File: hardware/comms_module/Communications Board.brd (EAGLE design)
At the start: 33.5 x 32.4 mm, 68 parts, among them U1 Value, U2 STC3115, X2 USB-MICROB, Y1 32.768kHz, Y2 24MHz

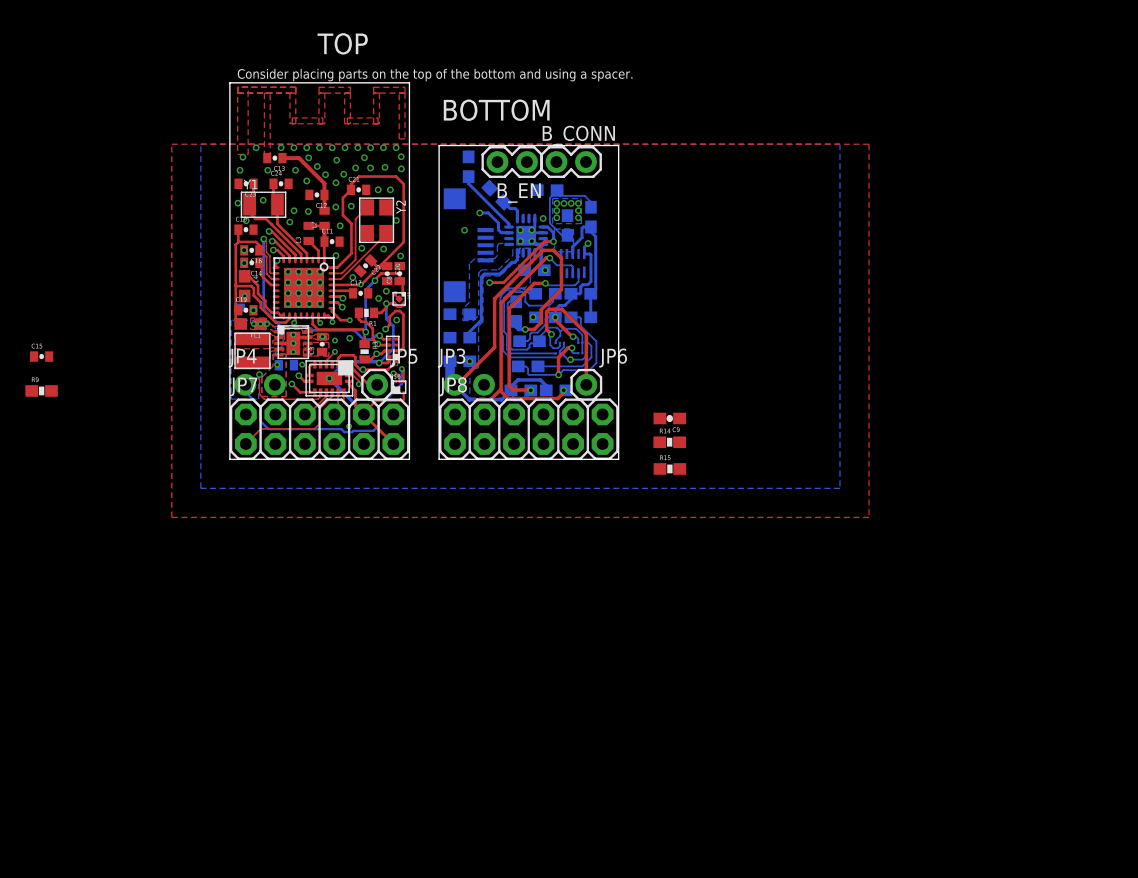
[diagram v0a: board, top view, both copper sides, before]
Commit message: Nearly complete routing. Add programming interface.
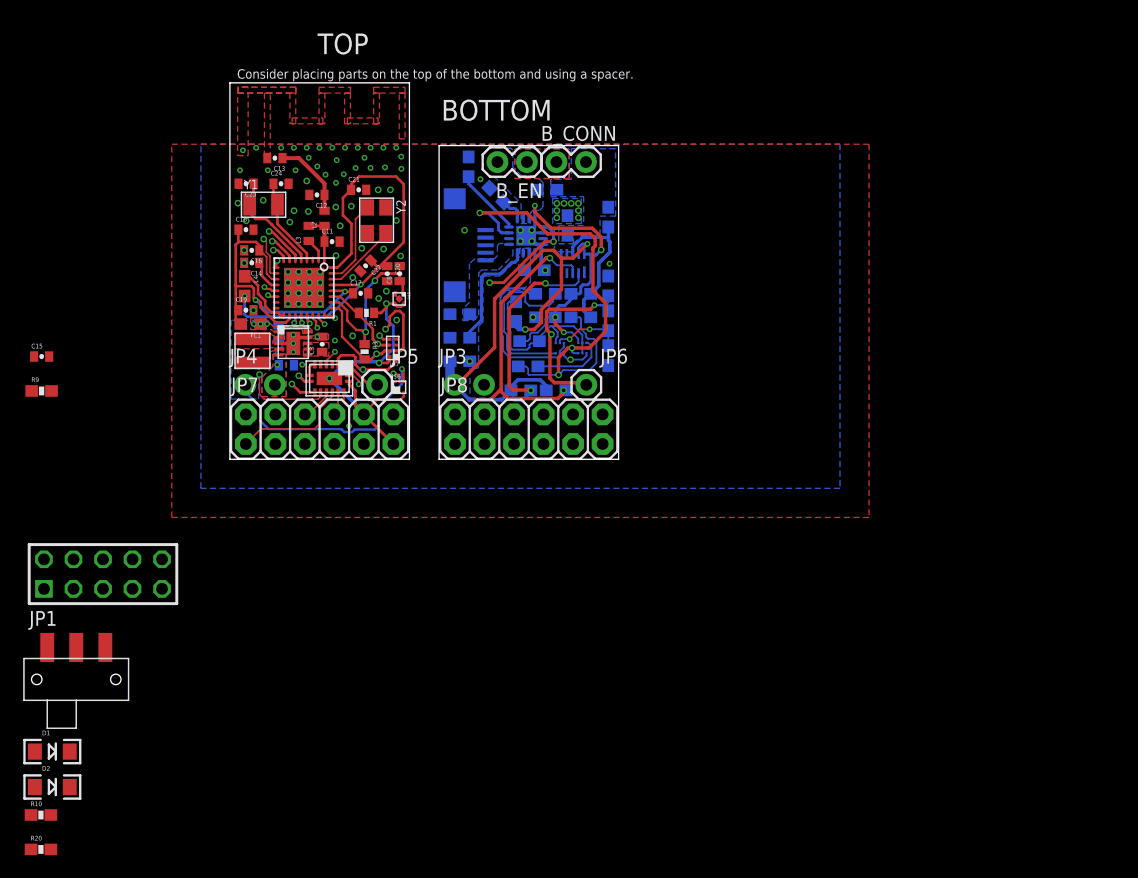
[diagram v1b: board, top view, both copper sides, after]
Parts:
- added D1: Green, SparkFun-LED:LED-1206
- added D2: Red, SparkFun-LED:LED-1206
- added JP1: AVR-JTAG-10, avr-7:AVR-JTAG-10
- added R10, R20: 500, SparkFun-Passives:0603-RES
- added S1: (no value), Capstone Library:JS102011SAQN
- C8: value (none) -> 1uF
- moved R15 13.8 mm to (32.6, 11.9), flipped to the bottom, turned to 270 degrees
- moved C9 12.6 mm to (32.6, 14.9), flipped to the bottom, turned to 90 degrees
- moved R14 9.13 mm to (32.6, 8.92), flipped to the bottom, turned to 270 degrees
- moved C7 3.68 mm to (4.19, 10.9)
- moved R4 1.49 mm to (32.6, 20.8)
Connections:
- removed net AGND: JP8.5
- removed net BATT_ALARM: U2.P1
- removed net JTAG_TDI: U1.16
- removed net JTAG_TDO: U1.15
- removed net N$25: JP8.9
- removed net N$26: JP8.8
- removed net N$27: JP8.6
- removed net N$28: JP8.3
- removed net N$29: JP8.1
- removed net TMR: U$2.14
- new net /SYSDISBL_PF: R14.1, R15.2, U$6.5
- new net N$14: D1.C, R10.1
- new net N$16: D2.C, R20.1
- new net N$6: D2.A, S1.3
- new net PROG_VCC: D1.A, JP1.7, S1.2
- net +1V3: now also U1.26; no longer U1.22
- net /SYSDISBL: no longer R14.1, R15.2, U$6.5
- net BANDAGE_A_0: now also JP8.6, U1.22; no longer U1.23
- net BANDAGE_A_1: now also JP8.3
- net BANDAGE_A_2: now also JP8.8
- net BANDAGE_A_3: now also JP8.1
- net BANDAGE_A_4: now also JP8.9
- net CONN_STATE_RD: now also U1.23; no longer U1.25
- net GND: now also JP1.10, JP1.2, JP8.5, R10.2, R20.2
- net JTAG_TCKC: now also JP1.1
- net JTAG_TSMC: now also JP1.5
- net MCU_RST: now also JP1.6; no longer U2.P7
- net SCL: now also U1.20; no longer U1.27
- net SDA: now also U1.21; no longer U1.26
- net VCC: now also JP1.4
- net VSENSE_0: now also U1.27; no longer U1.20
- net VSENSE_1: now also U1.25; no longer U1.21
- net V_PREBUCK: now also S1.1
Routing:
- net SYSOFF: track 20.6 -> 43.7 mm
- net VCC: track 23.2 -> 32.6 mm, vias 0 -> 2
- net BAT-: track 8.90 -> 0.00 mm
- net BAT+: track 16.9 -> 25.4 mm, vias 3 -> 4
- net +3V3: track 59.5 -> 65.7 mm, vias 5 -> 6
- net /SYSDISBL_PF: track 0.00 -> 6.14 mm, vias 0 -> 2
- net VSENSE_1: track 2.43 -> 8.31 mm
- net SCL: track 41.8 -> 37.8 mm
- net /SYSDISBL: track 16.7 -> 19.7 mm, vias 1 -> 2
- net MPSW: track 19.4 -> 22.3 mm
- net SDA: track 31.5 -> 28.8 mm
- net VSENSE_0: track 4.60 -> 7.28 mm
- net BATDC: track 11.5 -> 13.1 mm
- net JTAG_TSMC: track 0.00 -> 1.15 mm, vias 0 -> 1
- net +1V3: track 15.8 -> 14.7 mm
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- added copper zone on layer 1, net B+IN
- added copper zone on layer 16, net B+IN
- added copper zone on layer 16, net BAT+
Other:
- board text added: "Note: The distance from the top of the antenna to the board edge is increased due to the trace-dimension clearance of 15mil (0.381mm)"

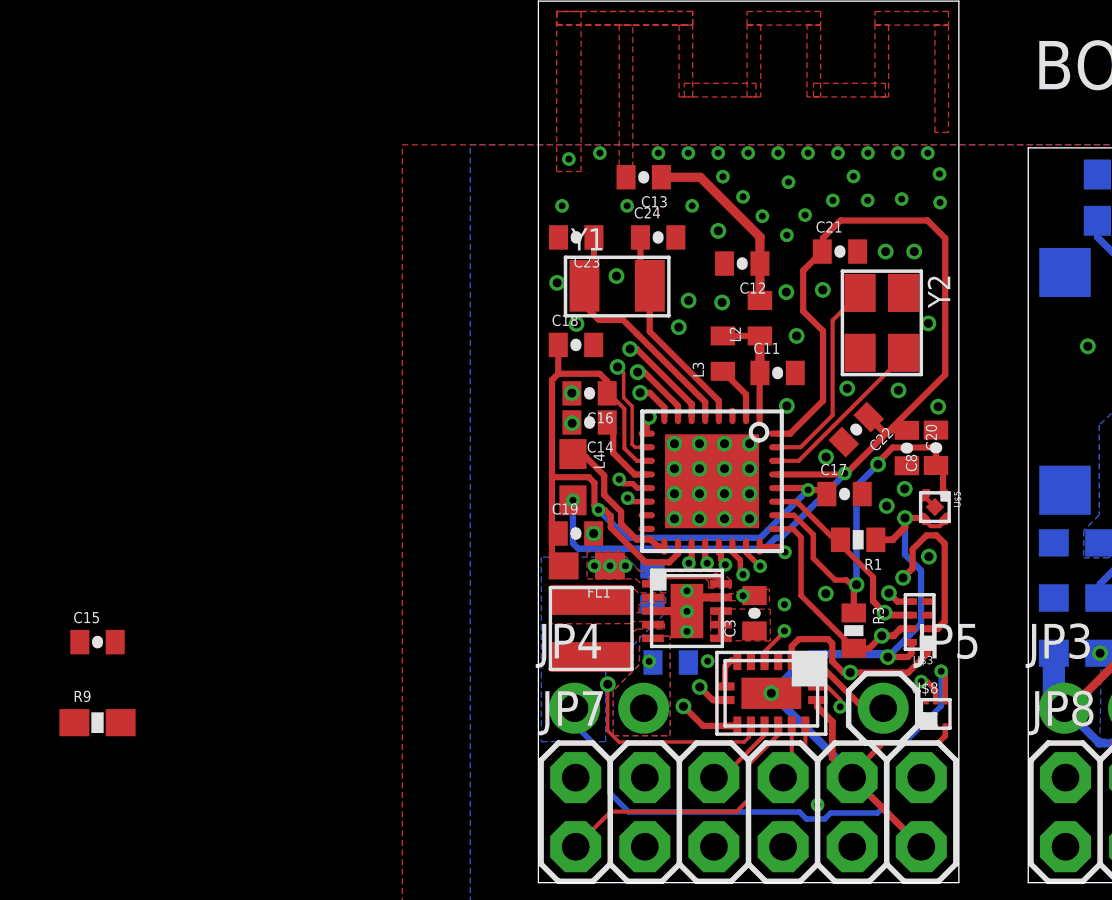
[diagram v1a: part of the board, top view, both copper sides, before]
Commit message: Continued routing of signals.
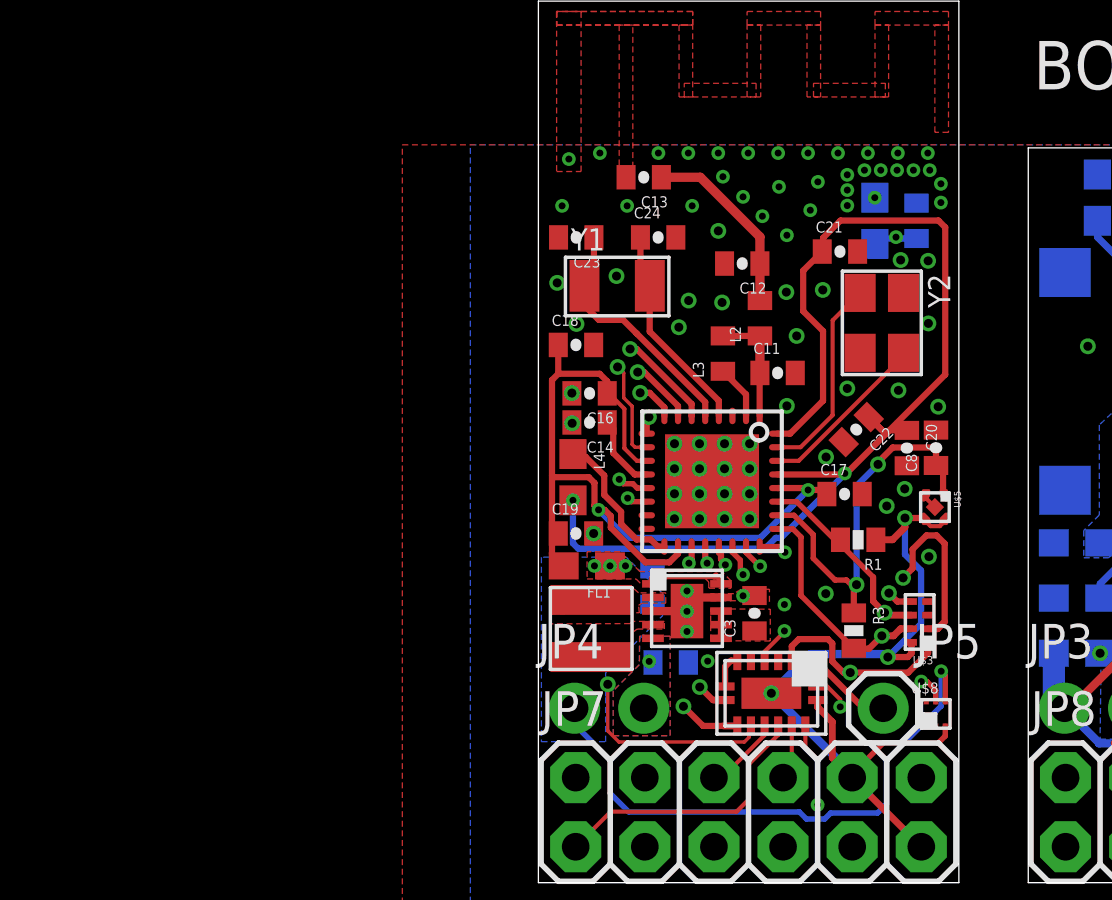
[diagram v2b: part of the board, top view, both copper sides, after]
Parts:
- moved R9 34.0 mm to (12.4, 24.3), flipped to the bottom, turned to 90 degrees
- moved C15 33.8 mm to (13.9, 24.3), flipped to the bottom, turned to 90 degrees
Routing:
- net MCU_RST: track 0.69 -> 29.5 mm, vias 1 -> 2
- net VCC: track 32.6 -> 47.3 mm, vias 2 -> 3
- net GND: vias 93 -> 98
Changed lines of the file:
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@@
 <element name="L3" library="SparkFun-Passives" package="C0402" value="15nH" x="6.78" y="19.44" rot="R90"/>
 <element name="C14" library="SparkFun-Passives" package="0402-CAP" value="1uF" x="1.88" y="16.91" rot="R180"/>
-<element name="C15" library="SparkFun-Passives" package="0402-CAP" value="100nF" x="-16.2" y="8.84"/>
-<element name="R9" library="SparkFun-Passives" package="0603-RES" value="100k" x="-16.2" y="5.88"/>
+<element name="C15" library="SparkFun-Passives" package="0402-CAP" value="100nF" x="13.89" y="24.32" rot="MR90"/>
+<element name="R9" library="SparkFun-Passives" package="0603-RES" value="100k" x="12.36" y="24.32" rot="MR90"/>
 <element name="C16" library="SparkFun-Passives" package="0402-CAP" value="100nF" x="1.88" y="17.98" rot="R180"/>
 <element name="C17" library="SparkFun-Passives" package="0402-CAP" value="100nF" x="11.25" y="14.28"/>
@@
 <via x="13.23" y="18.09" extent="1-16" drill="0.3302"/>
 <via x="10.57" y="15.64" extent="1-16" drill="0.3302"/>
-<via x="12.76" y="23.19" extent="1-16" drill="0.3302"/>
-<via x="13.81" y="23.19" extent="1-16" drill="0.3302"/>
+<via x="13.31" y="22.88" extent="1-16" drill="0.3302"/>
+<via x="14.32" y="22.85" extent="1-16" drill="0.3302"/>
 <via x="5" y="16.13" extent="1-16" drill="0.3302"/>
 <via x="5.92" y="16.13" extent="1-16" drill="0.3302"/>
@@
 <via x="14.69" y="17.49" extent="1-16" drill="0.3302"/>
 <via x="9.11" y="21.7" extent="1-16" drill="0.3302"/>
-<via x="9.8" y="24.53" extent="1-16" drill="0.254"/>
+<via x="9.99" y="24.71" extent="1-16" drill="0.254"/>
 <polygon width="0.1524" layer="2" rank="5">
 <vertex x="-3.92" y="-0.95"/>
@@
 <via x="5.16" y="20.41" extent="1-16" drill="0.3302"/>
 <via x="5.52" y="21.39" extent="1-16" drill="0.3302"/>
-<via x="10.82" y="25.07" extent="1-16" drill="0.254"/>
-<via x="12.1" y="25.07" extent="1-16" drill="0.254"/>
-<via x="13.35" y="25.12" extent="1-16" drill="0.254"/>
-<via x="14.76" y="24.99" extent="1-16" drill="0.254"/>
+<via x="10.27" y="25.75" extent="1-16" drill="0.254"/>
+<via x="12.58" y="26.18" extent="1-16" drill="0.254"/>
+<via x="13.78" y="26.18" extent="1-16" drill="0.254"/>
 <via x="6.78" y="25.94" extent="1-16" drill="0.254"/>
 <via x="7.52" y="25.2" extent="1-16" drill="0.254"/>
@@
 <via x="14.309" y="26.81" extent="1-16" drill="0.254"/>
 <via x="9.13" y="23.79" extent="1-16" drill="0.254"/>
-<via x="9.19" y="25.74" extent="1-16" drill="0.254"/>
-<via x="14.74" y="26.04" extent="1-16" drill="0.254"/>
-<via x="11.58" y="25.95" extent="1-16" drill="0.254"/>
+<via x="8.84" y="25.57" extent="1-16" drill="0.254"/>
+<via x="14.38" y="26.18" extent="1-16" drill="0.254"/>
+<via x="11.35" y="26.01" extent="1-16" drill="0.254"/>
 <contactref element="JP1" pad="10"/>
 <contactref element="R10" pad="2"/>
@@
 <via x="32.67" y="16.83" extent="1-16" drill="0.254"/>
 <via x="21.56" y="24.1" extent="1-16" drill="0.254"/>
+<via x="14.79" y="24.99" extent="1-16" drill="0.254"/>
+<via x="13.18" y="26.18" extent="1-16" drill="0.254"/>
+<via x="11.98" y="26.18" extent="1-16" drill="0.254"/>
+<via x="11.35" y="25.45" extent="1-16" drill="0.254"/>
+<via x="11.35" y="24.88" extent="1-16" drill="0.254"/>
+<via x="14.79" y="25.68" extent="1-16" drill="0.254"/>
 <wire x1="-15.41" y1="-30.61" x2="-15.41" y2="-33.57" width="0" layer="19" extent="1-1"/>
 <wire x1="-16" y1="-8.61" x2="-15.41" y2="-30.61" width="0" layer="19" extent="1-1"/>
@@
 <wire x1="6.38" y1="14.75" x2="6.84" y2="14.29" width="0" layer="19" extent="1-1"/>
 <wire x1="18.94" y1="12.49" x2="14.57" y2="13.8" width="0" layer="19" extent="1-16"/>
-<wire x1="-15.55" y1="8.84" x2="-16" y2="-8.61" width="0" layer="19" extent="1-1"/>
 </signal>
 <signal name="N$1">
@@
 <wire x1="5.130015625" y1="17.519984375" x2="3.89" y2="18.76" width="0.23" layer="1"/>
 <wire x1="3.89" y1="18.76" x2="3.65" y2="18.76" width="0.23" layer="1"/>
-<wire x1="0.53" y1="15.21" x2="0.53" y2="9.3" width="0.254" layer="2"/>
+<wire x1="0.53" y1="14.85" x2="0.53" y2="9.3" width="0.254" layer="2"/>
 <wire x1="0.53" y1="9.3" x2="2.54" y2="7.29" width="0.254" layer="2"/>
 <wire x1="2.54" y1="7.29" x2="2.55" y2="7.29" width="0.254" layer="2"/>
@@
 <wire x1="7.74" y1="5.34" x2="7.57" y2="5.17" width="0.127" layer="1"/>
 <wire x1="7.57" y1="5.17" x2="2.96" y2="5.17" width="0.127" layer="1"/>
-<wire x1="0.53" y1="15.21" x2="0.53" y2="15.64" width="0.23" layer="2"/>
-<wire x1="0.53" y1="15.64" x2="3.65" y2="18.76" width="0.23" layer="2"/>
+<wire x1="3.65" y1="18.76" x2="3.58" y2="18.76" width="0.23" layer="2"/>
+<wire x1="3.58" y1="18.76" x2="2.3" y2="17.48" width="0.23" layer="2"/>
+<wire x1="2.3" y1="17.48" x2="2.3" y2="16.62" width="0.23" layer="2"/>
+<wire x1="2.3" y1="16.62" x2="0.53" y2="14.85" width="0.23" layer="2"/>
 </signal>
 <signal name="MSW_1">
@@
 <wire x1="5.53" y1="11.77" x2="5.53" y2="11.73" width="0.2" layer="1"/>
 <contactref element="JP1" pad="6"/>
-<wire x1="-17.05" y1="5.88" x2="-10.92" y2="-8.61" width="0" layer="19" extent="1-1"/>
-<wire x1="-16.85" y1="8.84" x2="-17.05" y2="5.88" width="0" layer="19" extent="1-1"/>
-<wire x1="5.53" y1="11.74" x2="-16.85" y2="8.84" width="0" layer="19" extent="1-1"/>
+<wire x1="13.89" y1="23.67" x2="13.3" y2="23.67" width="0.23" layer="16"/>
+<wire x1="13.19" y1="23.67" x2="12.56" y2="23.67" width="0.23" layer="16"/>
+<wire x1="12.56" y1="23.67" x2="12.36" y2="23.47" width="0.23" layer="16"/>
+<via x="13.14" y="23.72" extent="1-16" drill="0.254"/>
+<wire x1="13.29" y1="23.68" x2="13.3" y2="23.67" width="0.23" layer="16"/>
+<wire x1="13.14" y1="23.72" x2="10.71" y2="23.72" width="0.23" layer="15"/>
+<wire x1="10.71" y1="23.72" x2="9.52" y2="22.53" width="0.23" layer="15"/>
+<wire x1="9.52" y1="22.53" x2="5" y2="22.53" width="0.23" layer="15"/>
+<wire x1="5" y1="22.53" x2="3.95" y2="21.48" width="0.23" layer="15"/>
+<wire x1="3.95" y1="21.48" x2="1.11" y2="21.48" width="0.23" layer="15"/>
+<wire x1="1.52" y1="12.2" x2="5.07" y2="12.2" width="0.23" layer="15"/>
+<wire x1="5.07" y1="12.2" x2="5.53" y2="11.74" width="0.23" layer="15"/>
+<wire x1="1.11" y1="21.48" x2="0.53" y2="20.9" width="0.23" layer="15"/>
+<wire x1="0.53" y1="20.9" x2="0.53" y2="13.19" width="0.23" layer="15"/>
+<wire x1="0.53" y1="13.19" x2="1.52" y2="12.2" width="0.23" layer="15"/>
+<wire x1="13.3" y1="23.67" x2="13.19" y2="23.67" width="0.23" layer="16"/>
+<wire x1="13.19" y1="23.67" x2="13.14" y2="23.72" width="0.23" layer="16"/>
+<wire x1="1.52" y1="12.2" x2="-10.92" y2="-8.61" width="0" layer="19" extent="1-15"/>
 </signal>
 <signal name="JTAG_TCKC">
@@
 <contactref element="C22" pad="1"/>
 <contactref element="L4" pad="2"/>
-<wire x1="14.95" y1="18.67" x2="14.95" y2="23.68" width="0.23" layer="1"/>
-<wire x1="14.95" y1="23.68" x2="14.3" y2="24.33" width="0.23" layer="1"/>
-<wire x1="14.3" y1="24.33" x2="11.1" y2="24.33" width="0.23" layer="1"/>
+<wire x1="14.95" y1="18.67" x2="14.95" y2="24.08" width="0.23" layer="1"/>
+<wire x1="14.7" y1="24.33" x2="11.1" y2="24.33" width="0.23" layer="1"/>
 <wire x1="11.1" y1="24.33" x2="10.46" y2="23.69" width="0.23" layer="1"/>
 <wire x1="10.46" y1="23.69" x2="10.46" y2="23.22" width="0.23" layer="1"/>
@@
 <wire x1="8.72" y1="12.67" x2="8.32" y2="12.27" width="0.23" layer="16"/>
 <wire x1="1.47" y1="12.27" x2="1.27" y2="12.47" width="0.23" layer="16"/>
+<wire x1="14.95" y1="24.08" x2="14.7" y2="24.33" width="0.23" layer="1"/>
 </signal>
 <signal name="RF_P">
@@
 <contactref element="JP1" pad="4"/>
 <wire x1="3.94" y1="11.77" x2="2.66" y2="13.05" width="0.23" layer="1"/>
-<wire x1="-15.35" y1="5.88" x2="-13.46" y2="-8.61" width="0" layer="19" extent="1-1"/>
-<wire x1="0.5" y1="12.07" x2="-15.35" y2="5.88" width="0" layer="19" extent="1-1"/>
+<via x="12.36" y="25.17" extent="1-16" drill="0.254"/>
+<wire x1="12.36" y1="25.17" x2="12.9" y2="25.17" width="0.23" layer="15"/>
+<wire x1="12.9" y1="25.17" x2="14.92" y2="23.15" width="0.23" layer="15"/>
+<wire x1="14.92" y1="23.15" x2="14.92" y2="22.36" width="0.23" layer="15"/>
+<wire x1="14.92" y1="22.36" x2="12.33" y2="19.77" width="0.23" layer="15"/>
+<wire x1="12.33" y1="19.77" x2="11.52" y2="19.77" width="0.23" layer="15"/>
+<wire x1="11.52" y1="19.77" x2="9.96" y2="18.21" width="0.23" layer="15"/>
+<wire x1="9.96" y1="18.21" x2="9.96" y2="14.48" width="0.23" layer="15"/>
+<wire x1="9.96" y1="14.48" x2="9.91" y2="14.43" width="0.23" layer="15"/>
+<wire x1="0.93" y1="11.64" x2="-13.46" y2="-8.61" width="0" layer="19" extent="1-1"/>
 </signal>
 <signal name="PERIPHERAL_DETECT">
